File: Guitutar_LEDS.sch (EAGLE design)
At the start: 161 parts

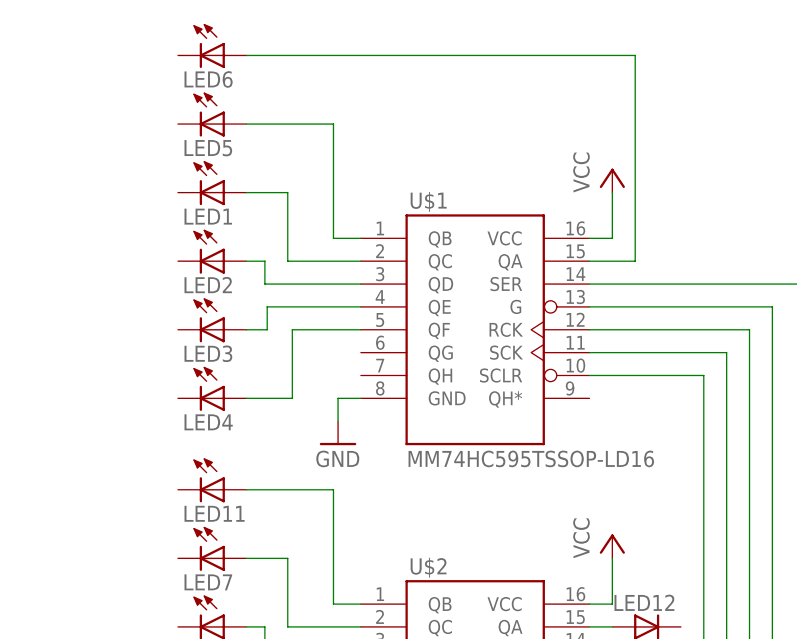
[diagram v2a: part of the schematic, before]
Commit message: Added series resistors to prevent overvoltage/overcurrent.
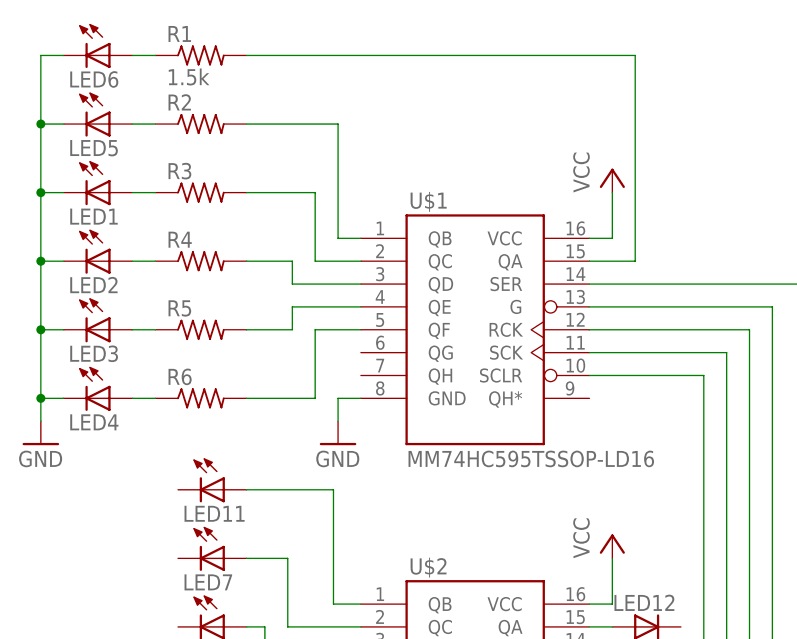
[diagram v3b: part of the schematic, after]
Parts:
- added R1: 1.5k, rcl:R-US_R0603
- added R2, R3, R4, R5, R6: (no value), rcl:R-US_R0603
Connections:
- new net N$166: LED6.A, R1.1
- new net N$168: LED4.A, R6.1
- new net N$169: LED3.A, R5.1
- new net N$170: LED2.A, R4.1
- new net N$171: LED1.A, R3.1
- new net N$172: LED5.A, R2.1
- net GND: now also LED1.C, LED2.C, LED3.C, LED4.C, LED5.C, LED6.C
- net N$1: now also R1.2, U$1.QA; no longer LED5.A, U$1.QB
- net N$2: now also R2.2, U$1.QB; no longer LED1.A, U$1.QC
- net N$3: now also R3.2, U$1.QC; no longer LED2.A, U$1.QD
- net N$4: now also R4.2, U$1.QD; no longer LED3.A, U$1.QE
- net N$5: now also R5.2, U$1.QE; no longer LED4.A, U$1.QF
- net N$6: now also R6.2, U$1.QF; no longer LED6.A, U$1.QA
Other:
- moved on the sheet: LED1, LED2, LED3, LED4, LED5, LED6
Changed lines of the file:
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@@
 <part name="P+23" library="supply1" deviceset="VCC" device=""/>
 <part name="U$1" library="ECE477_Guitutar" deviceset="MM74HC595" device="TSSOP-LD16"/>
+<part name="R1" library="rcl" deviceset="R-US_" device="R0603" value="1.5k"/>
+<part name="R2" library="rcl" deviceset="R-US_" device="R0603"/>
+<part name="R3" library="rcl" deviceset="R-US_" device="R0603"/>
+<part name="R4" library="rcl" deviceset="R-US_" device="R0603"/>
+<part name="R5" library="rcl" deviceset="R-US_" device="R0603"/>
+<part name="R6" library="rcl" deviceset="R-US_" device="R0603"/>
+<part name="GND24" library="supply1" deviceset="GND" device=""/>
 </parts>
 <sheets>
@@
 <instance part="FRAME1" gate="G$1" x="0" y="0"/>
 <instance part="FRAME1" gate="G$2" x="452.12" y="0"/>
-<instance part="LED1" gate="G$1" x="35.56" y="386.08" rot="R270"/>
-<instance part="LED2" gate="G$1" x="35.56" y="378.46" rot="R270"/>
-<instance part="LED3" gate="G$1" x="35.56" y="370.84" rot="R270"/>
-<instance part="LED4" gate="G$1" x="35.56" y="363.22" rot="R270"/>
-<instance part="LED5" gate="G$1" x="35.56" y="393.7" rot="R270"/>
-<instance part="LED6" gate="G$1" x="35.56" y="401.32" rot="R270"/>
+<instance part="LED1" gate="G$1" x="22.86" y="386.08" rot="R270"/>
+<instance part="LED2" gate="G$1" x="22.86" y="378.46" rot="R270"/>
+<instance part="LED3" gate="G$1" x="22.86" y="370.84" rot="R270"/>
+<instance part="LED4" gate="G$1" x="22.86" y="363.22" rot="R270"/>
+<instance part="LED5" gate="G$1" x="22.86" y="393.7" rot="R270"/>
+<instance part="LED6" gate="G$1" x="22.86" y="401.32" rot="R270"/>
 <instance part="GND1" gate="1" x="48.26" y="358.14"/>
 <instance part="P+1" gate="VCC" x="78.74" y="388.62"/>
@@
 <instance part="P+23" gate="VCC" x="256.54" y="142.24"/>
 <instance part="U$1" gate="G$1" x="63.5" y="370.84"/>
+<instance part="R1" gate="G$1" x="33.02" y="401.32"/>
+<instance part="R2" gate="G$1" x="33.02" y="393.7"/>
+<instance part="R3" gate="G$1" x="33.02" y="386.08"/>
+<instance part="R4" gate="G$1" x="33.02" y="378.46"/>
+<instance part="R5" gate="G$1" x="33.02" y="370.84"/>
+<instance part="R6" gate="G$1" x="33.02" y="363.22"/>
+<instance part="GND24" gate="1" x="15.24" y="358.14"/>
 </instances>
 <busses>
 </busses>
 <nets>
-<net name="N$1" class="0">
-<segment>
-<pinref part="LED5" gate="G$1" pin="A"/>
-<wire x1="38.1" y1="393.7" x2="47.752" y2="393.7" width="0.1524" layer="91"/>
-<wire x1="47.752" y1="393.7" x2="47.752" y2="381" width="0.1524" layer="91"/>
-<wire x1="47.752" y1="381" x2="50.8" y2="381" width="0.1524" layer="91"/>
-<pinref part="U$1" gate="G$1" pin="QB"/>
-</segment>
-</net>
-<net name="N$2" class="0">
-<segment>
-<pinref part="LED1" gate="G$1" pin="A"/>
-<wire x1="38.1" y1="386.08" x2="42.672" y2="386.08" width="0.1524" layer="91"/>
-<wire x1="42.672" y1="386.08" x2="42.672" y2="378.46" width="0.1524" layer="91"/>
-<wire x1="42.672" y1="378.46" x2="50.8" y2="378.46" width="0.1524" layer="91"/>
-<pinref part="U$1" gate="G$1" pin="QC"/>
-</segment>
-</net>
-<net name="N$3" class="0">
-<segment>
-<pinref part="LED2" gate="G$1" pin="A"/>
-<wire x1="38.1" y1="378.46" x2="40.132" y2="378.46" width="0.1524" layer="91"/>
-<wire x1="40.132" y1="378.46" x2="40.132" y2="375.92" width="0.1524" layer="91"/>
-<wire x1="40.132" y1="375.92" x2="50.8" y2="375.92" width="0.1524" layer="91"/>
-<pinref part="U$1" gate="G$1" pin="QD"/>
-</segment>
-</net>
-<net name="N$4" class="0">
-<segment>
-<pinref part="LED3" gate="G$1" pin="A"/>
-<wire x1="38.1" y1="370.84" x2="40.386" y2="370.84" width="0.1524" layer="91"/>
-<wire x1="40.386" y1="370.84" x2="40.386" y2="373.38" width="0.1524" layer="91"/>
-<wire x1="40.386" y1="373.38" x2="50.8" y2="373.38" width="0.1524" layer="91"/>
-<pinref part="U$1" gate="G$1" pin="QE"/>
-</segment>
-</net>
-<net name="N$5" class="0">
-<segment>
-<pinref part="LED4" gate="G$1" pin="A"/>
-<wire x1="38.1" y1="363.22" x2="43.18" y2="363.22" width="0.1524" layer="91"/>
-<wire x1="43.18" y1="363.22" x2="43.18" y2="370.84" width="0.1524" layer="91"/>
-<wire x1="43.18" y1="370.84" x2="50.8" y2="370.84" width="0.1524" layer="91"/>
-<pinref part="U$1" gate="G$1" pin="QF"/>
-</segment>
-</net>
 <net name="GND" class="0">
 <segment>
@@
 <pinref part="U$23" gate="G$1" pin="GND"/>
 <wire x1="226.06" y1="116.84" x2="228.6" y2="116.84" width="0.1524" layer="91"/>
+</segment>
+<segment>
+<pinref part="LED6" gate="G$1" pin="C"/>
+<pinref part="GND24" gate="1" pin="GND"/>
+<wire x1="17.78" y1="401.32" x2="15.24" y2="401.32" width="0.1524" layer="91"/>
+<wire x1="15.24" y1="401.32" x2="15.24" y2="393.7" width="0.1524" layer="91"/>
+<pinref part="LED4" gate="G$1" pin="C"/>
+<wire x1="15.24" y1="393.7" x2="15.24" y2="386.08" width="0.1524" layer="91"/>
+<wire x1="15.24" y1="386.08" x2="15.24" y2="378.46" width="0.1524" layer="91"/>
+<wire x1="15.24" y1="378.46" x2="15.24" y2="370.84" width="0.1524" layer="91"/>
+<wire x1="15.24" y1="370.84" x2="15.24" y2="363.22" width="0.1524" layer="91"/>
+<wire x1="15.24" y1="363.22" x2="15.24" y2="360.68" width="0.1524" layer="91"/>
+<wire x1="17.78" y1="363.22" x2="15.24" y2="363.22" width="0.1524" layer="91"/>
+<pinref part="LED3" gate="G$1" pin="C"/>
+<wire x1="17.78" y1="370.84" x2="15.24" y2="370.84" width="0.1524" layer="91"/>
+<pinref part="LED2" gate="G$1" pin="C"/>
+<wire x1="17.78" y1="378.46" x2="15.24" y2="378.46" width="0.1524" layer="91"/>
+<pinref part="LED1" gate="G$1" pin="C"/>
+<wire x1="17.78" y1="386.08" x2="15.24" y2="386.08" width="0.1524" layer="91"/>
+<pinref part="LED5" gate="G$1" pin="C"/>
+<wire x1="17.78" y1="393.7" x2="15.24" y2="393.7" width="0.1524" layer="91"/>
+<junction x="15.24" y="393.7"/>
+<junction x="15.24" y="386.08"/>
+<junction x="15.24" y="378.46"/>
+<junction x="15.24" y="370.84"/>
+<junction x="15.24" y="363.22"/>
 </segment>
 </net>
@@
 </segment>
 </net>
+<net name="N$166" class="0">
+<segment>
+<pinref part="LED6" gate="G$1" pin="A"/>
+<pinref part="R1" gate="G$1" pin="1"/>
+<wire x1="25.4" y1="401.32" x2="27.94" y2="401.32" width="0.1524" layer="91"/>
+</segment>
+</net>
+<net name="N$168" class="0">
+<segment>
+<pinref part="R6" gate="G$1" pin="1"/>
+<pinref part="LED4" gate="G$1" pin="A"/>
+<wire x1="27.94" y1="363.22" x2="25.4" y2="363.22" width="0.1524" layer="91"/>
+</segment>
+</net>
+<net name="N$169" class="0">
+<segment>
+<pinref part="R5" gate="G$1" pin="1"/>
+<pinref part="LED3" gate="G$1" pin="A"/>
+<wire x1="27.94" y1="370.84" x2="25.4" y2="370.84" width="0.1524" layer="91"/>
+</segment>
+</net>
+<net name="N$170" class="0">
+<segment>
+<pinref part="R4" gate="G$1" pin="1"/>
+<pinref part="LED2" gate="G$1" pin="A"/>
+<wire x1="27.94" y1="378.46" x2="25.4" y2="378.46" width="0.1524" layer="91"/>
+</segment>
+</net>
+<net name="N$171" class="0">
+<segment>
+<pinref part="R3" gate="G$1" pin="1"/>
+<pinref part="LED1" gate="G$1" pin="A"/>
+<wire x1="27.94" y1="386.08" x2="25.4" y2="386.08" width="0.1524" layer="91"/>
+</segment>
+</net>
+<net name="N$172" class="0">
+<segment>
+<pinref part="R2" gate="G$1" pin="1"/>
+<pinref part="LED5" gate="G$1" pin="A"/>
+<wire x1="27.94" y1="393.7" x2="25.4" y2="393.7" width="0.1524" layer="91"/>
+</segment>
+</net>
+<net name="N$1" class="0">
+<segment>
+<pinref part="R1" gate="G$1" pin="2"/>
+<wire x1="38.1" y1="401.32" x2="81.28" y2="401.32" width="0.1524" layer="91"/>
+<wire x1="81.28" y1="401.32" x2="81.28" y2="378.46" width="0.1524" layer="91"/>
+<pinref part="U$1" gate="G$1" pin="QA"/>
+<wire x1="81.28" y1="378.46" x2="76.2" y2="378.46" width="0.1524" layer="91"/>
+</segment>
+</net>
+<net name="N$2" class="0">
+<segment>
+<pinref part="R2" gate="G$1" pin="2"/>
+<wire x1="38.1" y1="393.7" x2="48.26" y2="393.7" width="0.1524" layer="91"/>
+<wire x1="48.26" y1="393.7" x2="48.26" y2="381" width="0.1524" layer="91"/>
+<pinref part="U$1" gate="G$1" pin="QB"/>
+<wire x1="48.26" y1="381" x2="50.8" y2="381" width="0.1524" layer="91"/>
+</segment>
+</net>
+<net name="N$3" class="0">
+<segment>
+<pinref part="R3" gate="G$1" pin="2"/>
+<wire x1="38.1" y1="386.08" x2="45.72" y2="386.08" width="0.1524" layer="91"/>
+<wire x1="45.72" y1="386.08" x2="45.72" y2="378.46" width="0.1524" layer="91"/>
+<pinref part="U$1" gate="G$1" pin="QC"/>
+<wire x1="45.72" y1="378.46" x2="50.8" y2="378.46" width="0.1524" layer="91"/>
+</segment>
+</net>
+<net name="N$4" class="0">
+<segment>
+<pinref part="R4" gate="G$1" pin="2"/>
+<wire x1="38.1" y1="378.46" x2="43.18" y2="378.46" width="0.1524" layer="91"/>
+<wire x1="43.18" y1="378.46" x2="43.18" y2="375.92" width="0.1524" layer="91"/>
+<pinref part="U$1" gate="G$1" pin="QD"/>
+<wire x1="43.18" y1="375.92" x2="50.8" y2="375.92" width="0.1524" layer="91"/>
+</segment>
+</net>
+<net name="N$5" class="0">
+<segment>
+<pinref part="U$1" gate="G$1" pin="QE"/>
+<wire x1="43.18" y1="373.38" x2="50.8" y2="373.38" width="0.1524" layer="91"/>
+<pinref part="R5" gate="G$1" pin="2"/>
+<wire x1="38.1" y1="370.84" x2="43.18" y2="370.84" width="0.1524" layer="91"/>
+<wire x1="43.18" y1="370.84" x2="43.18" y2="373.38" width="0.1524" layer="91"/>
+</segment>
+</net>
 <net name="N$6" class="0">
 <segment>
-<pinref part="U$1" gate="G$1" pin="QA"/>
-<wire x1="76.2" y1="378.46" x2="81.28" y2="378.46" width="0.1524" layer="91"/>
-<wire x1="81.28" y1="378.46" x2="81.28" y2="401.32" width="0.1524" layer="91"/>
-<pinref part="LED6" gate="G$1" pin="A"/>
-<wire x1="81.28" y1="401.32" x2="38.1" y2="401.32" width="0.1524" layer="91"/>
-</segment>
-</net>
+<pinref part="R6" gate="G$1" pin="2"/>
+<wire x1="38.1" y1="363.22" x2="45.72" y2="363.22" width="0.1524" layer="91"/>
+<wire x1="45.72" y1="363.22" x2="45.72" y2="370.84" width="0.1524" layer="91"/>
+<pinref part="U$1" gate="G$1" pin="QF"/>
+<wire x1="45.72" y1="370.84" x2="50.8" y2="370.84" width="0.1524" layer="91"/>
+</segment>
+</net>
